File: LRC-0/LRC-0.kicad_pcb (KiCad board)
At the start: 2 copper layers, 8 parts, among them U1 ESP32-C6-MINI-1, U2 SX1262IMLTRT, U3 TVS1400DRV, U4 NCP1117-3.3_SOT223, U5 TP4056-42-ESOP8, U6 BQ24075RGT, Y1 TX32-33015S-32.000-X-R

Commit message: schematic
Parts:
- added C1: 10u, Capacitor_SMD:C_0402_1005Metric, F.Cu at (39.4, 51.1)
- added C12: 100n, Capacitor_SMD:C_0402_1005Metric, F.Cu at (168.5, 131.0)
- added C15: 100n, Capacitor_SMD:C_0402_1005Metric, F.Cu at (125.1, 48.6)
- added C16: 100n, Capacitor_SMD:C_0402_1005Metric, F.Cu at (125.1, 50.6)
- added C17: 470n, Capacitor_SMD:C_0402_1005Metric, F.Cu at (125.1, 52.5)
- added C18: 47n, Capacitor_SMD:C_0402_1005Metric, F.Cu at (125.1, 54.5)
- added C19: 47p, Capacitor_SMD:C_0402_1005Metric, F.Cu at (125.1, 56.5)
- added C2: 10u, Capacitor_SMD:C_0402_1005Metric, F.Cu at (39.4, 53.1)
- added C20: 1u, Capacitor_SMD:C_0402_1005Metric, F.Cu at (125.1, 58.5)
- added C21: 100p, Capacitor_SMD:C_0402_1005Metric, F.Cu at (209.5, 75.0)
- added C22: 100n, Capacitor_SMD:C_0402_1005Metric, F.Cu at (209.5, 77.0)
- added C23: 100n, Capacitor_SMD:C_0402_1005Metric, F.Cu at (205.3, 95.9)
- added C3: 100n, Capacitor_SMD:C_0402_1005Metric, F.Cu at (118.9, 145.4)
- added C4: 4.7u, Capacitor_SMD:C_0402_1005Metric, F.Cu at (92.5, 52.1)
- added C5: 100n, Capacitor_SMD:C_0402_1005Metric, F.Cu at (118.9, 147.4)
- added C6: 4.7u, Capacitor_SMD:C_0402_1005Metric, F.Cu at (92.5, 54.1)
- added C7: 4.7u, Capacitor_SMD:C_0402_1005Metric, F.Cu at (92.5, 56.0)
- added C8: 4.7u, Capacitor_SMD:C_0402_1005Metric, F.Cu at (92.5, 58.0)
- added D1: LED, LED_SMD:LED_0805_2012Metric, F.Cu at (92.2, 45.5)
- added D2: LED, LED_SMD:LED_0805_2012Metric, F.Cu at (92.2, 48.5)
- added FB1: 600@100MHz, Inductor_SMD:L_0603_1608Metric, F.Cu at (165.1, 131.3)
- added J1: USB_C_Receptacle_USB2.0_14P, Connector_USB:USB_C_Receptacle_GCT_USB4105-xx-A_16P_TopMnt_Horizontal, F.Cu at (42.2, 119.8)
- added J2: Battery, Connector_PinHeader_2.54mm:PinHeader_1x02_P2.54mm_Vertical, F.Cu at (87.7, 46.3)
- added J3: SMA, Connector_Coaxial:SMA_Amphenol_132289_EdgeMount, F.Cu at (177.6, 116.4)
- added J4: u.FL, Connector_Coaxial:U.FL_Hirose_U.FL-R-SMT-1_Vertical, F.Cu at (183.0, 125.5)
- added J5: Conn_01x10, Connector_PinHeader_2.54mm:PinHeader_1x10_P2.54mm_Vertical, F.Cu at (168.0, 42.8)
- added L1: 47n, Inductor_SMD:L_0402_1005Metric, F.Cu at (128.0, 54.9)
- added L2: 15u, Inductor_SMD:L_0402_1005Metric, F.Cu at (128.0, 56.9)
- added R1: 5.1k, Resistor_SMD:R_0402_1005Metric, F.Cu at (37.8, 125.5)
- added R10: 1k, Resistor_SMD:R_0402_1005Metric, F.Cu at (84.0, 54.9)
- added R13: 10k, Resistor_SMD:R_0402_1005Metric, F.Cu at (128.0, 58.9)
- added R17: 47, Resistor_SMD:R_0402_1005Metric, F.Cu at (205.2, 79.3)
- added R2: 5.1k, Resistor_SMD:R_0402_1005Metric, F.Cu at (37.8, 127.5)
- added R3: 10k, Resistor_SMD:R_0402_1005Metric, F.Cu at (118.9, 141.4)
- added R4: 39k, Resistor_SMD:R_0402_1005Metric, F.Cu at (84.0, 45.0)
- added R5: 1k, Resistor_SMD:R_0402_1005Metric, F.Cu at (84.0, 47.0)
- added R6: 1.2k, Resistor_SMD:R_0402_1005Metric, F.Cu at (84.0, 48.9)
- added R7: 10k, Resistor_SMD:R_0402_1005Metric, F.Cu at (118.9, 143.4)
- added R8: 10k, Resistor_SMD:R_0402_1005Metric, F.Cu at (84.0, 50.9)
- added R9: 1k, Resistor_SMD:R_0402_1005Metric, F.Cu at (84.0, 52.9)
- added SW1: EN, Button_Switch_SMD:SW_Push_SPST_NO_Alps_SKRK, F.Cu at (114.2, 142.7)
- added SW2: BOOT, Button_Switch_SMD:SW_Push_SPST_NO_Alps_SKRK, F.Cu at (114.2, 147.1)
- added U7: RFSW1012TR7, Package_DFN_QFN:LQFN-12-1EP_2x2mm_P0.5mm_EP0.7x0.7mm, F.Cu at (206.0, 92.8)
- U1: value ESP32-C6-MINI-1 -> AP7361C-33E; footprint ESP32_C6_MINI_1U_H4:XCVR_ESP32-C6-MINI-1U-H4 -> Package_TO_SOT_SMD:SOT-223-3_TabPin2
- U2: value SX1262IMLTRT -> TVS1400DRV; footprint Package_DFN_QFN:QFN-24-1EP_4x4mm_P0.5mm_EP2.6x2.6mm -> Package_SON:WSON-6-1EP_2x2mm_P0.65mm_EP1x1.6mm
- U3: value TVS1400DRV -> BQ24075RGT; footprint Package_SON:WSON-6-1EP_2x2mm_P0.65mm_EP1x1.6mm -> Package_DFN_QFN:VQFN-16-1EP_3x3mm_P0.5mm_EP1.6x1.6mm
- U4: value NCP1117-3.3_SOT223 -> ESP32-C6-MINI-1; footprint Package_TO_SOT_SMD:SOT-223-3_TabPin2 -> RF_Module:ESP32-C6-MINI-1
- U5: value TP4056-42-ESOP8 -> SX1262IMLTRT; footprint Package_SO:SOIC-8-1EP_3.9x4.9mm_P1.27mm_EP2.41x3.3mm_ThermalVias -> Package_DFN_QFN:QFN-24-1EP_4x4mm_P0.5mm_EP2.6x2.6mm
- U6: value BQ24075RGT -> RFSW1012TR7; footprint Package_DFN_QFN:VQFN-16-1EP_3x3mm_P0.5mm_EP1.6x1.6mm -> Package_DFN_QFN:LQFN-12-1EP_2x2mm_P0.5mm_EP0.7x0.7mm
- moved U1 129.9 mm to (42.9, 46.0)
- moved U2 128.4 mm to (41.1, 126.3)
- moved U3 98.4 mm to (88.4, 53.8)
- moved U5 65.1 mm to (130.1, 50.8)
- moved U6 54.4 mm to (205.9, 76.2)
- moved FL1 37.0 mm to (209.0, 118.9)
- moved U4 26.9 mm to (133.1, 134.1)
- moved Y1 12.4 mm to (165.7, 127.5)
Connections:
- FL1 pad 10: Net-(FL1-GND-Pad10) -> GND
- FL1 pad 2: Net-(FL1-GND-Pad10) -> GND
- FL1 pad 5: Net-(FL1-GND-Pad10) -> GND
- FL1 pad 6: unconnected-(FL1-SW_RFI-Pad6) -> /RF1
- FL1 pad 7: Net-(FL1-GND-Pad10) -> GND
- FL1 pad 8: unconnected-(FL1-SW_RFO-Pad8) -> /RF2
- FL1 pad 9: Net-(FL1-GND-Pad10) -> GND
- U1 pad 1: GND -> VCC
- U2 pad 1: +3V3 -> GND
- U2 pad 3: /XTA -> GND
- U2 pad 4: /XTB -> +5V
- U2 pad 5: GND -> +5V
- U2 pad 6: unconnected-(U2-DIO3-Pad6) -> +5V
- U2 pad 7: unconnected-(U2-VREG-Pad7) -> GND
- U3 pad 1: GND -> Net-(U3-TS)
- U3 pad 2: GND -> /BAT+
- U3 pad 3: GND -> /BAT+
- U3 pad 4: VCC -> GND
- U3 pad 5: VCC -> +5V
- U3 pad 6: VCC -> GND
- U3 pad 7: GND -> Net-(D2-K)
- U4 pad 2: +3V3 -> GND
- U4 pad 3: VCC -> +3V3
- U5 pad 1: GND -> +3V3
- U5 pad 2: Net-(U5-PROG) -> GND
- U5 pad 3: GND -> /XTA
- U5 pad 4: +5V -> unconnected-(U5-XTB-Pad4)
- U5 pad 5: /BAT+ -> GND
- U5 pad 6: Net-(U5-~{STDBY}) -> /DIO3
- U5 pad 8: +5V -> GND
- U5 pad 9: GND -> Net-(U5-DCC_SW)
- U6 pad 1: Net-(U6-TS) -> GND
- U6 pad 10: VCC -> GND
- U6 pad 11: VCC -> /RF2
- U6 pad 12: Net-(U6-ILIM) -> GND
- U6 pad 13: +5V -> unconnected-(U6-EP-Pad13)
- U6 pad 2: /BAT+ -> Net-(U6-RFC)
- U6 pad 3: /BAT+ -> GND
- U6 pad 5: GND -> /RF1
- U6 pad 6: VCC -> GND
- U6 pad 8: GND -> Net-(U6-EN)
- U6 pad 9: Net-(D3-K) -> +3V3
- Y1 pad 3: /XTB -> Net-(Y1-OUTPUT)
- Y1 pad 4: /XTA -> Net-(Y1-VDC)

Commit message: pi filters
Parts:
- moved FL1 240.5 mm to (0.00, 0.00)
- moved C23 226.6 mm to (0.00, 0.00)
- moved U7 226.0 mm to (0.00, 0.00)
- moved C22 223.2 mm to (0.00, 0.00)
- moved C21 222.5 mm to (0.00, 0.00)
- moved J4 221.9 mm to (0.00, 0.00)
- moved R17 220.0 mm to (0.00, 0.00)
- moved U6 219.6 mm to (0.00, 0.00)
- moved C12 213.4 mm to (0.00, 0.00)
- moved J3 212.3 mm to (0.00, 0.00)
- moved FB1 210.9 mm to (0.00, 0.00)
- moved Y1 209.0 mm to (0.00, 0.00)
- moved C5 189.4 mm to (0.00, 0.00)
- moved U4 188.9 mm to (0.00, 0.00)
- moved C3 187.8 mm to (0.00, 0.00)
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
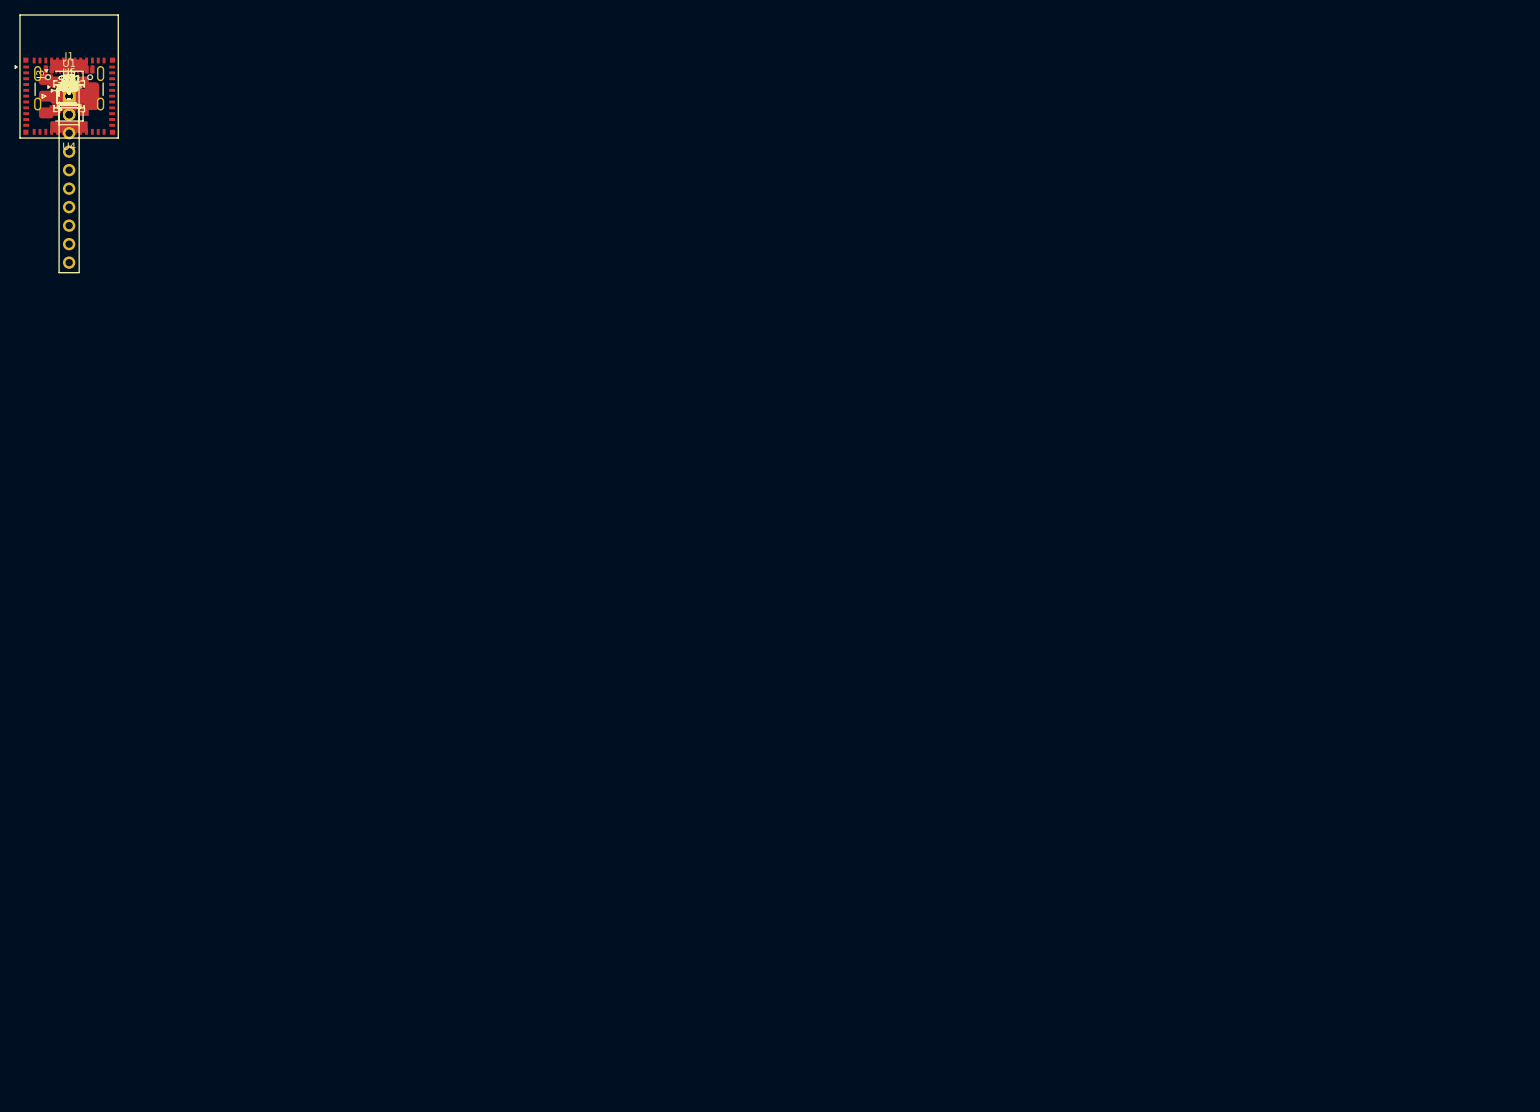
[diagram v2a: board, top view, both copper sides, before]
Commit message: removed pi filters, pcb started
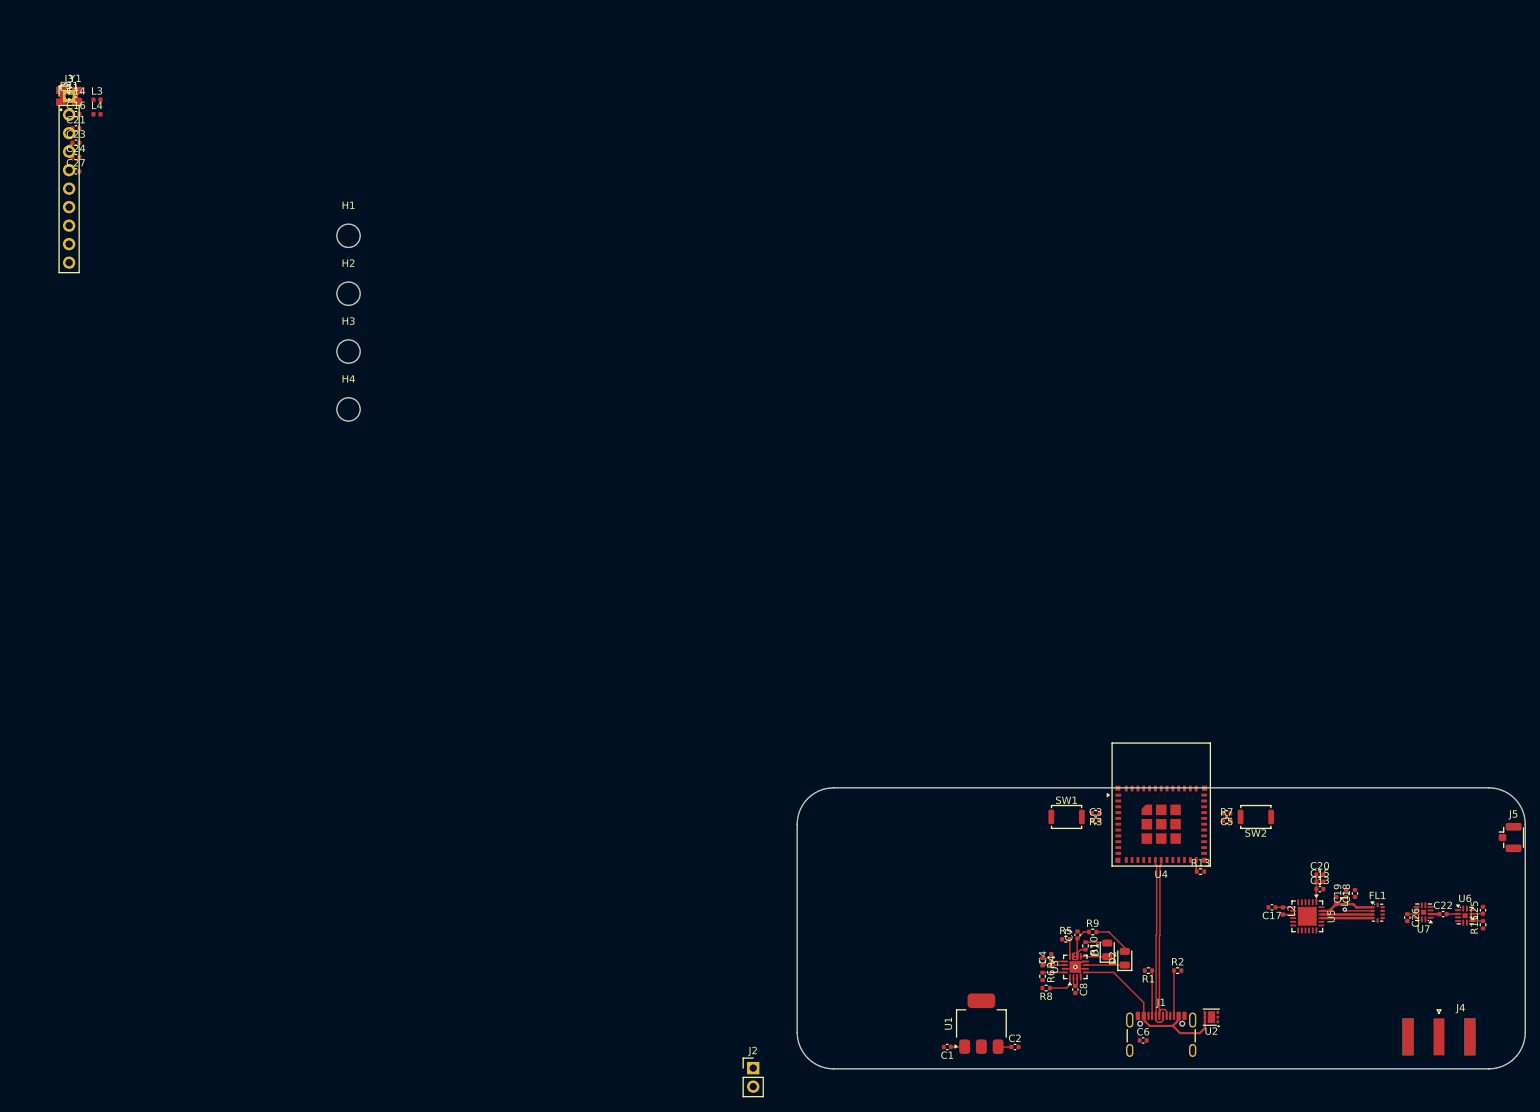
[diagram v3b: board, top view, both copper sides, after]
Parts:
- added C14: C, Capacitor_SMD:C_0402_1005Metric, F.Cu at (0.94, 0.48)
- added C16: C, Capacitor_SMD:C_0402_1005Metric, F.Cu at (0.94, 2.46)
- added C21: C, Capacitor_SMD:C_0402_1005Metric, F.Cu at (0.94, 4.42)
- added C23: 47n, Capacitor_SMD:C_0402_1005Metric, F.Cu at (0.94, 6.39)
- added C24: C, Capacitor_SMD:C_0402_1005Metric, F.Cu at (0.94, 8.37)
- added C27: C, Capacitor_SMD:C_0402_1005Metric, F.Cu at (0.94, 10.3)
- added H1: MountingHole_Pad, MountingHole:MountingHole_3.2mm_M3, F.Cu at (38.4, 19.2)
- added H2: MountingHole_Pad, MountingHole:MountingHole_3.2mm_M3, F.Cu at (38.4, 27.1)
- added H3: MountingHole_Pad, MountingHole:MountingHole_3.2mm_M3, F.Cu at (38.4, 35.1)
- added H4: MountingHole_Pad, MountingHole:MountingHole_3.2mm_M3, F.Cu at (38.4, 43.0)
- added L3: L, Inductor_SMD:L_0402_1005Metric, F.Cu at (3.83, 0.49)
- added L4: L, Inductor_SMD:L_0402_1005Metric, F.Cu at (3.83, 2.48)
- moved J4 228.2 mm to (188.2, 129.2), turned to -90 degrees
- moved R15 225.1 mm to (194.2, 113.8), turned to 90 degrees
- moved C25 224.1 mm to (194.2, 111.8), turned to 90 degrees
- moved J5 223.0 mm to (198.4, 101.8)
- moved U6 222.3 mm to (191.7, 112.5)
- moved C22 219.6 mm to (188.7, 112.3)
- moved U7 217.2 mm to (186.0, 112.1), turned to 180 degrees
- moved C26 215.7 mm to (183.8, 112.8), turned to -90 degrees
- moved FL1 211.8 mm to (179.7, 112.2)
- moved C18 207.8 mm to (176.6, 109.5), turned to 90 degrees
- moved C19 206.8 mm to (175.4, 109.5), turned to 90 degrees
- moved L1 206.1 mm to (174.0, 110.5), turned to -90 degrees
- moved U5 204.0 mm to (170.1, 112.7), turned to -90 degrees
- moved C13 203.4 mm to (171.8, 108.9)
- moved C15 202.9 mm to (171.8, 107.9)
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- renumbered C12 to C11, C15 to C13, C16 to C15, C21 to C22, C22 to C25, C23 to C26, J5 to J3, J3 to J4, J4 to J5, R17 to R15
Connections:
- U4 pad 10: /LED -> unconnected-(U4-IO5-Pad10)
- U4 pad 13: /RST -> unconnected-(U4-IO1-Pad13)
- U4 pad 15: /T_IRQ -> unconnected-(U4-IO6-Pad15)
- U4 pad 5: /DC -> unconnected-(U4-IO2-Pad5)
- U4 pad 6: /MOSI_{D} -> unconnected-(U4-IO3-Pad6)
- U4 pad 9: /MISO_{D} -> unconnected-(U4-IO4-Pad9)
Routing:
- net +5V: track 0.00 -> 27.3 mm
- net /D-: track 0.00 -> 24.0 mm
- net /D+: track 0.00 -> 24.0 mm
- net GND: track 0.00 -> 10.5 mm, vias 0 -> 2
- net VCC: track 0.00 -> 8.68 mm
- net +3V3: track 0.00 -> 8.51 mm
- net /RFO: track 0.00 -> 7.57 mm
- net /RFI_N: track 0.00 -> 7.01 mm
- net /RFI_P: track 0.00 -> 7.00 mm
- net Net-(J1-CC2): track 0.00 -> 6.22 mm
- net Net-(J1-CC1): track 0.00 -> 6.22 mm
- net Net-(D2-K): track 0.00 -> 5.36 mm
- net Net-(D2-A): track 0.00 -> 5.28 mm
- net Net-(U3-TS): track 0.00 -> 3.95 mm
- net Net-(D1-K): track 0.00 -> 3.65 mm
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- added copper zone on F.Cu, net VCC
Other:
- board outline added: 100 x 38.6 mm
- copper layers 2 -> 4
